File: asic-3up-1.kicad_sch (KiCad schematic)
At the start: 81 parts, among them U10 BM1362AC_MODE1, U12 MCP1824T-1202E/OT, U13 MCP1824T-0802E, U14 MCP1824T-1202E/OT, U15 MCP1824T-0802E, U4 MCP1824T-1202E/OT, U5 MCP1824T-0802E, U8 BM1362AC_MODE1, U9 BM1362AC_MODE0

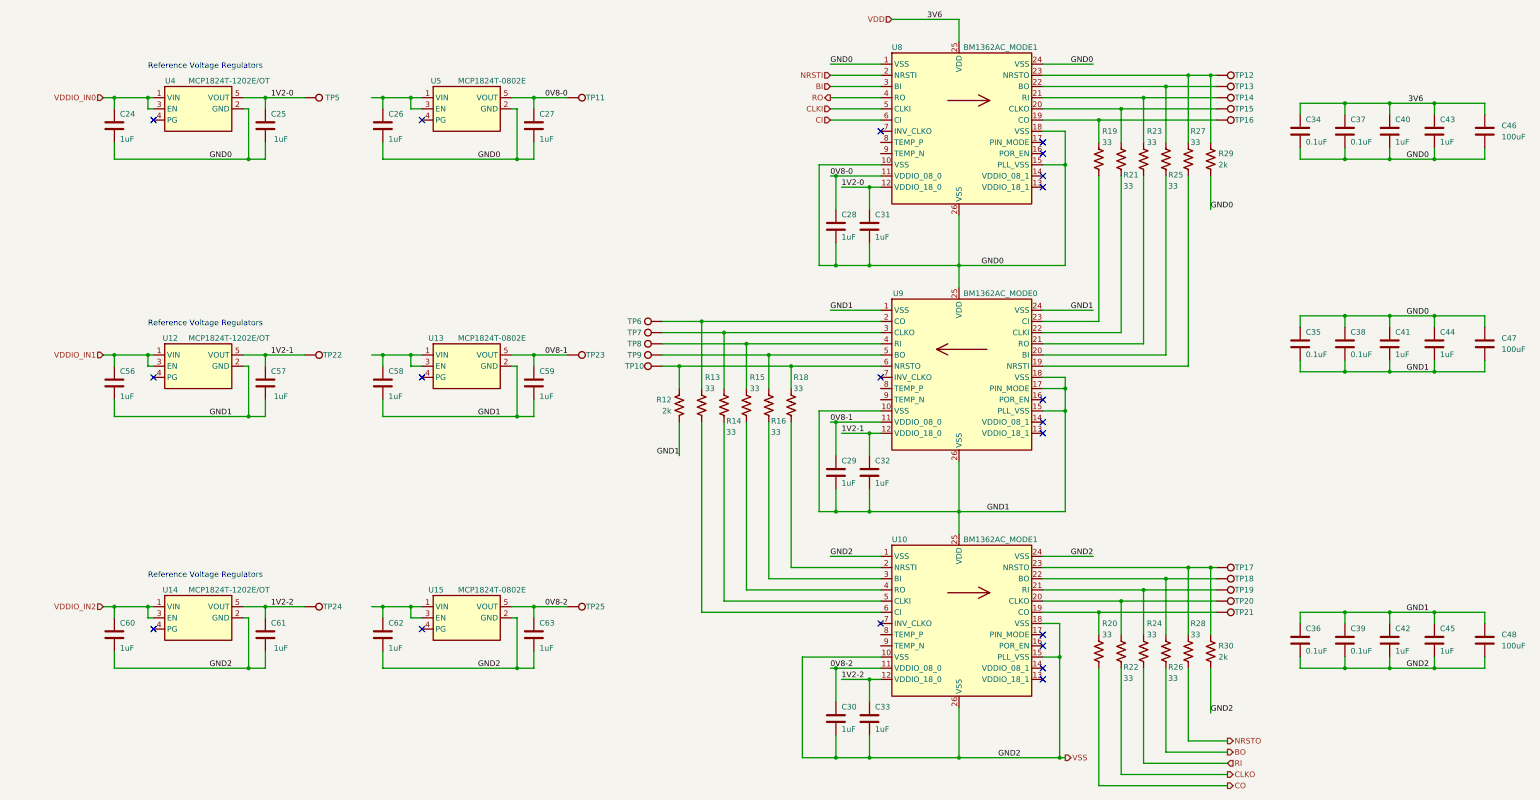
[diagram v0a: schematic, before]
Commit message: added sweet logo to schematic worksheet. Schematic cleanup.
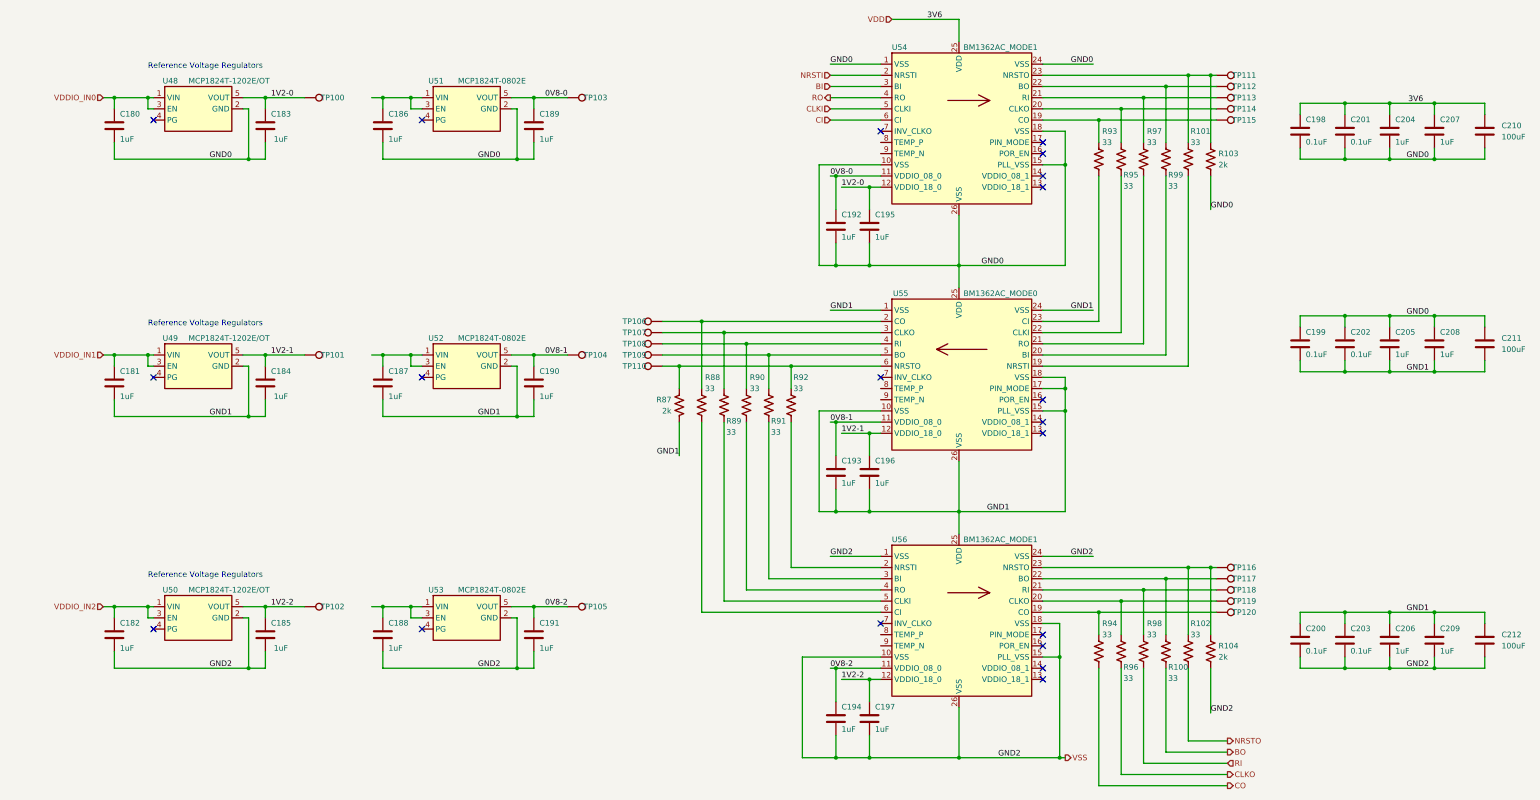
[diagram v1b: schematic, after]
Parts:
- renumbered C24 to C180, C56 to C181, C60 to C182, C25 to C183, C57 to C184, C61 to C185, C26 to C186, C58 to C187, C62 to C188, C27 to C189, C59 to C190, C63 to C191, C28 to C192, C29 to C193, C30 to C194, C31 to C195, C32 to C196, C33 to C197, C34 to C198, C35 to C199, C36 to C200, C37 to C201, C38 to C202, C39 to C203, C40 to C204, C41 to C205, C42 to C206, C43 to C207, C44 to C208, C45 to C209, C46 to C210, C47 to C211, C48 to C212, R26 to R100, R27 to R101, R28 to R102, R29 to R103, R30 to R104, R12 to R87, R13 to R88, R14 to R89, R15 to R90, R16 to R91, R18 to R92, R19 to R93, R20 to R94, R21 to R95, R22 to R96, R23 to R97, R24 to R98, R25 to R99, TP5 to TP100, TP22 to TP101, TP24 to TP102, TP11 to TP103, TP23 to TP104, TP25 to TP105, TP6 to TP106, TP7 to TP107, TP8 to TP108, TP9 to TP109, TP10 to TP110, TP12 to TP111, TP13 to TP112, TP14 to TP113, TP15 to TP114, TP16 to TP115, TP17 to TP116, TP18 to TP117, TP19 to TP118, TP20 to TP119, TP21 to TP120, U4 to U48, U12 to U49, U14 to U50, U5 to U51, U13 to U52, U15 to U53, U8 to U54, U9 to U55, U10 to U56

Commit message: starting layout
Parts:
- added J5, J7: Conn_01x01, emberone:5x9_powertab, symbol Connector_Generic:Conn_01x01
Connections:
- net GND0: now also J5.1 (Pin_1)
- net GND1: now also J7.1 (Pin_1)
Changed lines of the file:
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@@
 	)
 	(junction
+		(at 248.92 153.67)
+		(diameter 0)
+		(color 0 0 0 0)
+	)
+	(junction
 		(at 346.71 115.57)
 		(diameter 0.9144)
@@
 	)
 	(junction
+		(at 248.92 99.06)
+		(diameter 0)
+		(color 0 0 0 0)
+	)
+	(junction
 		(at 148.59 195.58)
 		(diameter 0.9144)
@@
 	(wire
 		(pts
+			(xy 248.92 153.67) (xy 248.92 160.02)
+		)
+		(stroke
+			(width 0)
+			(type default)
+		)
+	)
+	(wire
+		(pts
 			(xy 368.3 125.73) (xy 368.3 128.27)
 		)
@@
 	(wire
 		(pts
-			(xy 248.92 92.71) (xy 248.92 104.14)
+			(xy 248.92 92.71) (xy 248.92 99.06)
 		)
 		(stroke
@@
 	(wire
 		(pts
-			(xy 248.92 148.59) (xy 248.92 160.02)
+			(xy 248.92 148.59) (xy 248.92 153.67)
 		)
 		(stroke
@@
 	(wire
 		(pts
+			(xy 248.92 99.06) (xy 248.92 104.14)
+		)
+		(stroke
+			(width 0)
+			(type default)
+		)
+	)
+	(wire
+		(pts
 			(xy 273.05 160.02) (xy 273.05 137.16)
 		)
@@
 	)
 	(symbol
+		(lib_id "Connector_Generic:Conn_01x01")
+		(at 254 99.06 0)
+		(unit 1)
+		(exclude_from_sim no)
+		(in_bom yes)
+		(on_board yes)
+		(dnp no)
+		(property "Reference" "J5"
+			(at 256.286 99.06 0)
+			(effects
+				(font
+					(size 1.27 1.27)
+				)
+				(justify left)
+			)
+		)
+		(property "Value" "Conn_01x01"
+			(at 256.54 100.3299 0)
+			(effects
+				(font
+					(size 1.27 1.27)
+				)
+				(justify left)
+				(hide yes)
+			)
+		)
+		(property "Footprint" "emberone:5x9_powertab"
+			(at 254 99.06 0)
+			(effects
+				(font
+					(size 1.27 1.27)
+				)
+				(hide yes)
+			)
+		)
+		(property "Datasheet" "~"
+			(at 254 99.06 0)
+			(effects
+				(font
+					(size 1.27 1.27)
+				)
+				(hide yes)
+			)
+		)
+		(property "Description" "powertab"
+			(at 254 99.06 0)
+			(effects
+				(font
+					(size 1.27 1.27)
+				)
+				(hide yes)
+			)
+		)
+		(pin "1"
+		)
+		(instances
+			(project "emberone"
+				(path "/b036224c-4cdf-48cc-81df-19bc5283ebd2/1041e984-4167-4ef3-8410-dcacf0440a69"
+					(reference "J5")
+					(unit 1)
+				)
+			)
+		)
+	)
+	(symbol
 		(lib_id "emberone:BM1362AC_MODE1")
 		(at 248.92 72.39 0)
@@
 					(unit 1)
 				)
+			)
+		)
+	)
+	(symbol
+		(lib_id "Connector_Generic:Conn_01x01")
+		(at 254 153.67 0)
+		(unit 1)
+		(exclude_from_sim no)
+		(in_bom yes)
+		(on_board yes)
+		(dnp no)
+		(property "Reference" "J7"
+			(at 256.286 153.67 0)
+			(effects
+				(font
+					(size 1.27 1.27)
+				)
+				(justify left)
+			)
+		)
+		(property "Value" "Conn_01x01"
+			(at 256.54 154.9399 0)
+			(effects
+				(font
+					(size 1.27 1.27)
+				)
+				(justify left)
+				(hide yes)
+			)
+		)
+		(property "Footprint" "emberone:5x9_powertab"
+			(at 254 153.67 0)
+			(effects
+				(font
+					(size 1.27 1.27)
+				)
+				(hide yes)
+			)
+		)
+		(property "Datasheet" "~"
+			(at 254 153.67 0)
+			(effects
+				(font
+					(size 1.27 1.27)
+				)
+				(hide yes)
+			)
+		)
+		(property "Description" "powertab"
+			(at 254 153.67 0)
+			(effects
+				(font
+					(size 1.27 1.27)
+				)
+				(hide yes)
+			)
+		)
+		(pin "1"
+		)
+		(instances
+			(project "emberone"
+				(path "/b036224c-4cdf-48cc-81df-19bc5283ebd2/1041e984-4167-4ef3-8410-dcacf0440a69"
+					(reference "J7")
+					(unit 1)
+				)

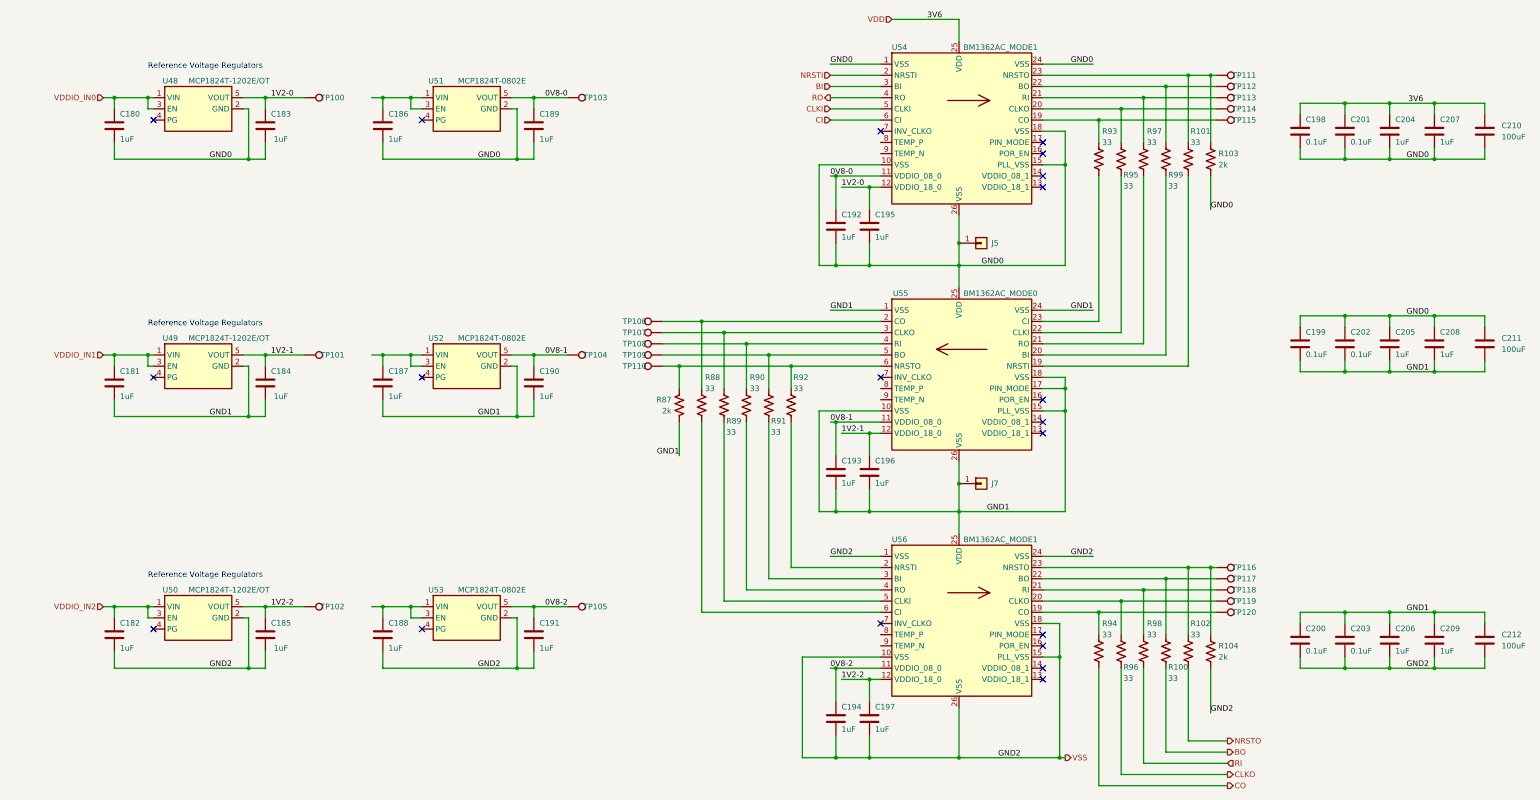
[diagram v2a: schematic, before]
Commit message: so much placing. added mask and paste opening on ASIC footprints. added a pad for a rear heatsink
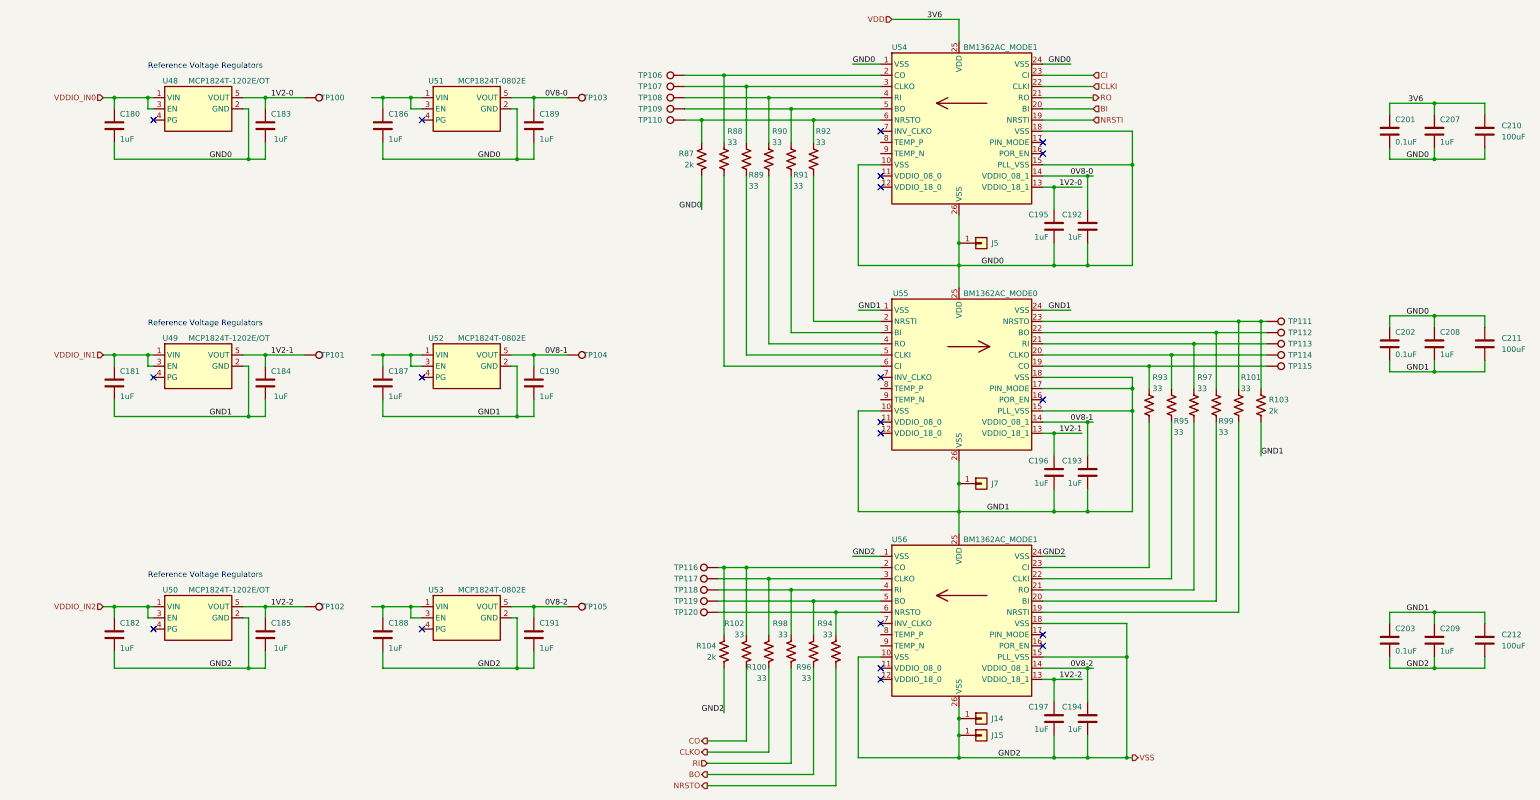
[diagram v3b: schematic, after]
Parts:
- removed C198, C199, C200: 0.1uF, Capacitor_SMD:C_0402_1005Metric, symbol Device:C
- removed C204, C205, C206: 1uF, Capacitor_SMD:C_0402_1005Metric, symbol Device:C
- added J14: Conn_01x01, emberone:14x9_powertab_L, symbol Connector_Generic:Conn_01x01
- added J15: Conn_01x01, emberone:14x9_powertab_R, symbol Connector_Generic:Conn_01x01
- U54, U56: symbol emberone:BM1362AC_MODE1 -> emberone:BM1362AC_MODE0
- U55: symbol emberone:BM1362AC_MODE0 -> emberone:BM1362AC_MODE1
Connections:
- net 0V8-0: now also U54.14 (VDDIO_08_1); no longer U54.11 (VDDIO_08_0)
- net 0V8-1: now also U55.14 (VDDIO_08_1); no longer U55.11 (VDDIO_08_0)
- net 0V8-2: now also U56.14 (VDDIO_08_1); no longer U56.11 (VDDIO_08_0)
- net 1V2-0: now also U54.13 (VDDIO_18_1); no longer U54.12 (VDDIO_18_0)
- net 1V2-1: now also U55.13 (VDDIO_18_1); no longer U55.12 (VDDIO_18_0)
- net 1V2-2: now also U56.13 (VDDIO_18_1); no longer U56.12 (VDDIO_18_0)
- net BI: now also U54.20 (BI); no longer U54.3 (BI)
- net BO: now also R96.2; no longer R100.2
- net CI: now also U54.23 (CI); no longer U54.6 (CI)
- net CLKI: now also U54.22 (CLKI); no longer U54.5 (CLKI)
- net CLKO: now also R100.2; no longer R96.2
- net CO: now also R102.2; no longer R94.2
- net GND0: now also R87.2; no longer R103.2
- net GND1: now also R103.2; no longer R87.2
- net NRSTI: now also U54.19 (NRSTI); no longer U54.2 (NRSTI)
- net NRSTO: now also R94.2; no longer R102.2
- net RO: now also U54.21 (RO); no longer U54.4 (RO)
- net VSS: now also J14.1 (Pin_1), J15.1 (Pin_1)
- net at R101.1, R103.1, TP111.1: now also U55.23 (NRSTO); no longer U54.23 (NRSTO)
- net at R88.1, TP106.1: now also U54.2 (CO); no longer U55.2 (CO)
- net at R95.1, TP114.1: now also U55.20 (CLKO); no longer U54.20 (CLKO)
- net at R95.2: now also U56.22 (CLKI); no longer U55.22 (CLKI)
- net at R93.1, TP115.1: now also U55.19 (CO); no longer U54.19 (CO)
- net at R101.2: now also U56.19 (NRSTI); no longer U55.19 (NRSTI)
- net at R102.1, R104.1, TP116.1: now also U56.2 (CO); no longer U56.23 (NRSTO)
- net at R87.1, R92.1, TP110.1: now also U54.6 (NRSTO); no longer U55.6 (NRSTO)
- net at R92.2: now also U55.2 (NRSTI); no longer U56.2 (NRSTI)
- net at R99.1, TP112.1: now also U55.22 (BO); no longer U54.22 (BO)
- net at R96.1, TP119.1: now also U56.5 (BO); no longer U56.20 (CLKO)
- net at R97.1, TP113.1: now also U55.21 (RI); no longer U54.21 (RI)
- net at R94.1, TP120.1: now also U56.6 (NRSTO); no longer U56.19 (CO)
- net at R98.1, TP118.1: now also U56.4 (RI); no longer U56.21 (RI)
- net at R100.1, TP117.1: now also U56.3 (CLKO); no longer U56.22 (BO)
- net at R99.2: now also U56.20 (BI); no longer U55.20 (BI)
- net at R97.2: now also U56.21 (RO); no longer U55.21 (RO)
- net at R93.2: now also U56.23 (CI); no longer U55.23 (CI)
- net at R89.1, TP107.1: now also U54.3 (CLKO); no longer U55.3 (CLKO)
- net at R90.1, TP108.1: now also U54.4 (RI); no longer U55.4 (RI)
- net at R91.1, TP109.1: now also U54.5 (BO); no longer U55.5 (BO)
- net at R91.2: now also U55.3 (BI); no longer U56.3 (BI)
- net at R90.2: now also U55.4 (RO); no longer U56.4 (RO)
- net at R89.2: now also U55.5 (CLKI); no longer U56.5 (CLKI)
- net at R88.2: now also U55.6 (CI); no longer U56.6 (CI)
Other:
- moved on the sheet: C192, C193, C194, C195, C196, C197, C201, C202, C203, R100, R101, R102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

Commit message: forgot that data needs to start with the ASIC that has GND at system GND... reversed everything
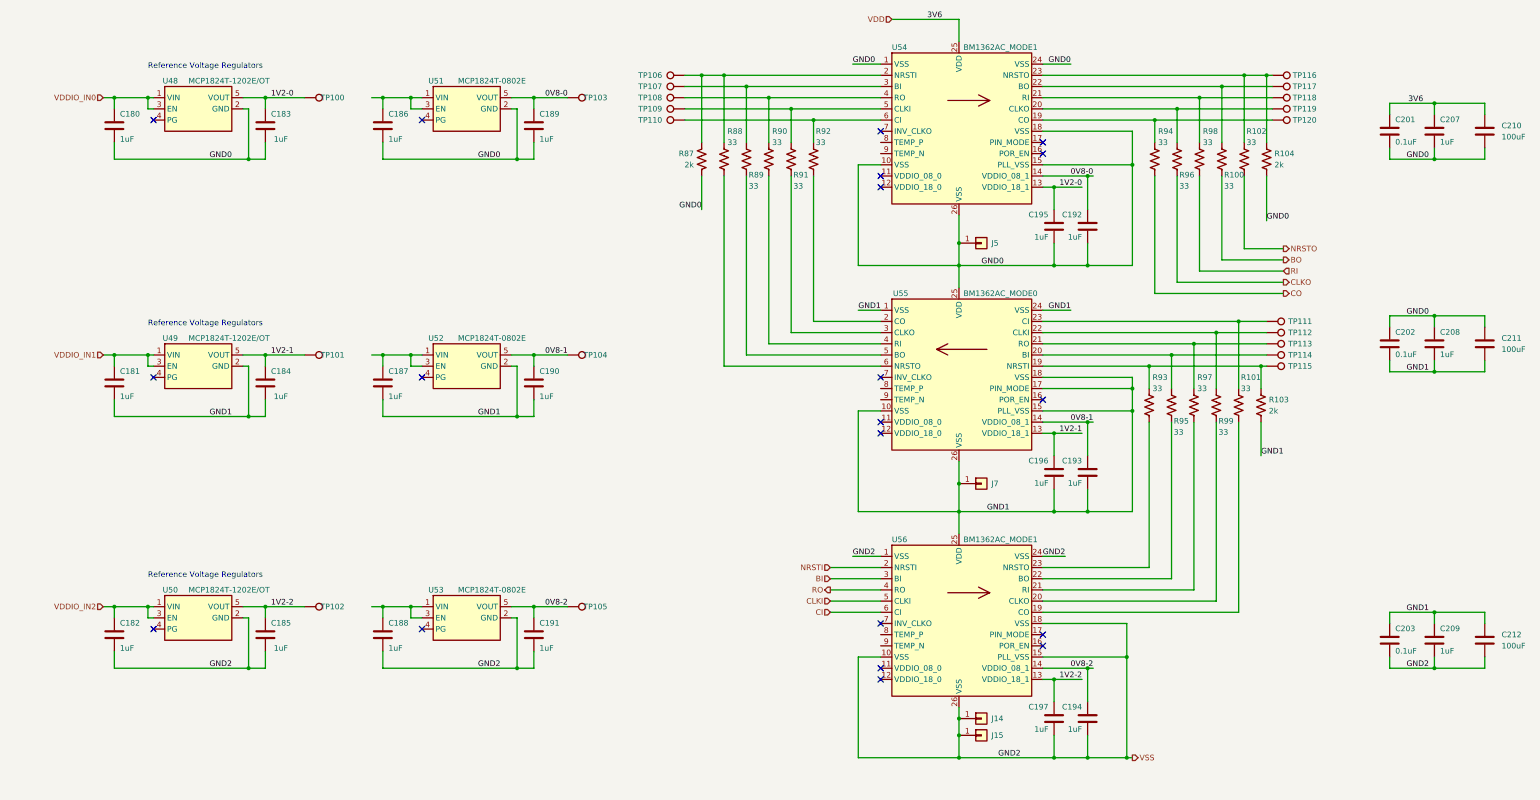
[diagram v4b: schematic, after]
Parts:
- U54, U56: symbol emberone:BM1362AC_MODE0 -> emberone:BM1362AC_MODE1
- U55: symbol emberone:BM1362AC_MODE1 -> emberone:BM1362AC_MODE0
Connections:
- net BI: now also U56.3 (BI); no longer U54.20 (BI)
- net BO: now also R100.2; no longer R96.2
- net CI: now also U56.6 (CI); no longer U54.23 (CI)
- net CLKI: now also U56.5 (CLKI); no longer U54.22 (CLKI)
- net CLKO: now also R96.2; no longer R100.2
- net CO: now also R94.2; no longer R102.2
- net GND0: now also R104.2
- net NRSTI: now also U56.2 (NRSTI); no longer U54.19 (NRSTI)
- net NRSTO: now also R102.2; no longer R94.2
- net RO: now also U56.4 (RO); no longer U54.21 (RO)
- net VSS: no longer R104.2
- net at R101.1, TP111.1, U55.23 (CI): no longer R103.1
- net at R88.1, TP106.1, U54.2 (NRSTI): now also R87.1
- net at R93.1, TP115.1, U55.19 (NRSTI): now also R103.1
- net at R102.1, R104.1, TP116.1: now also U54.23 (NRSTO); no longer U56.2 (CO)
- net at R92.1, TP110.1, U54.6 (CI): no longer R87.1
- net at R96.1, TP119.1: now also U54.20 (CLKO); no longer U56.5 (BO)
- net at R94.1, TP120.1: now also U54.19 (CO); no longer U56.6 (NRSTO)
- net at R98.1, TP118.1: now also U54.21 (RI); no longer U56.4 (RI)
- net at R100.1, TP117.1: now also U54.22 (BO); no longer U56.3 (CLKO)
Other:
- moved on the sheet: R100, R102, R104, R94, R96, R98, TP116, TP117, TP118, TP119, TP120
